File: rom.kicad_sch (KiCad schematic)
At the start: 5 parts, among them IC17 27C256, IC18 74LS08

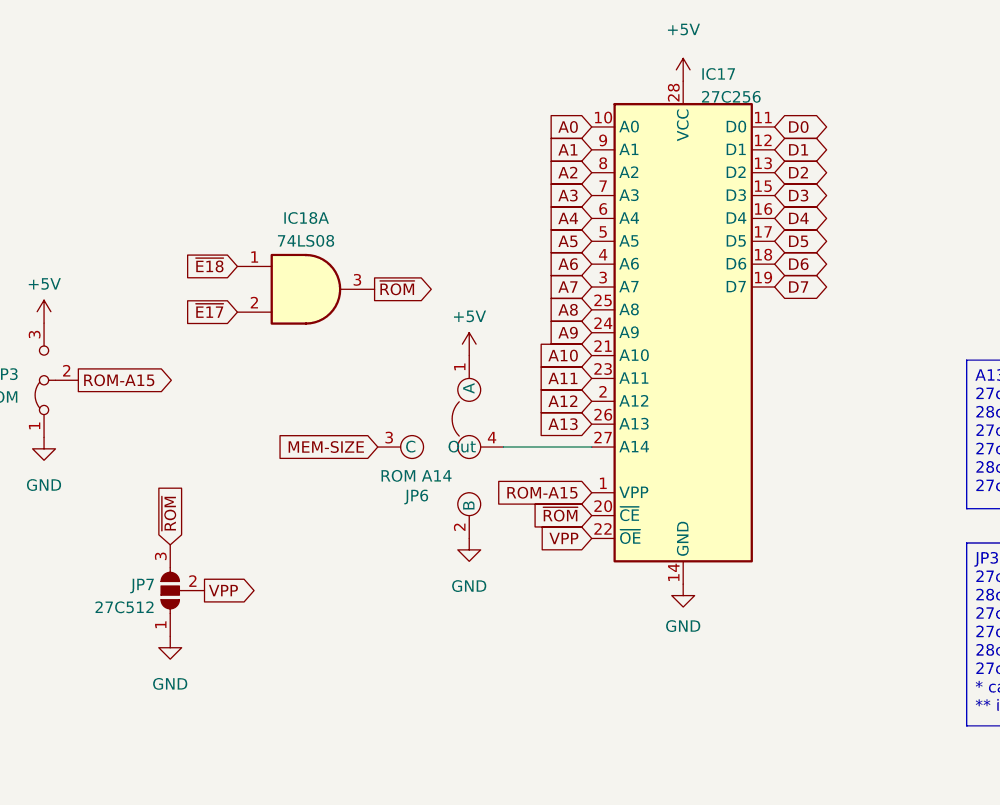
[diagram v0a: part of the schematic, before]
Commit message: rework keyboard type selection
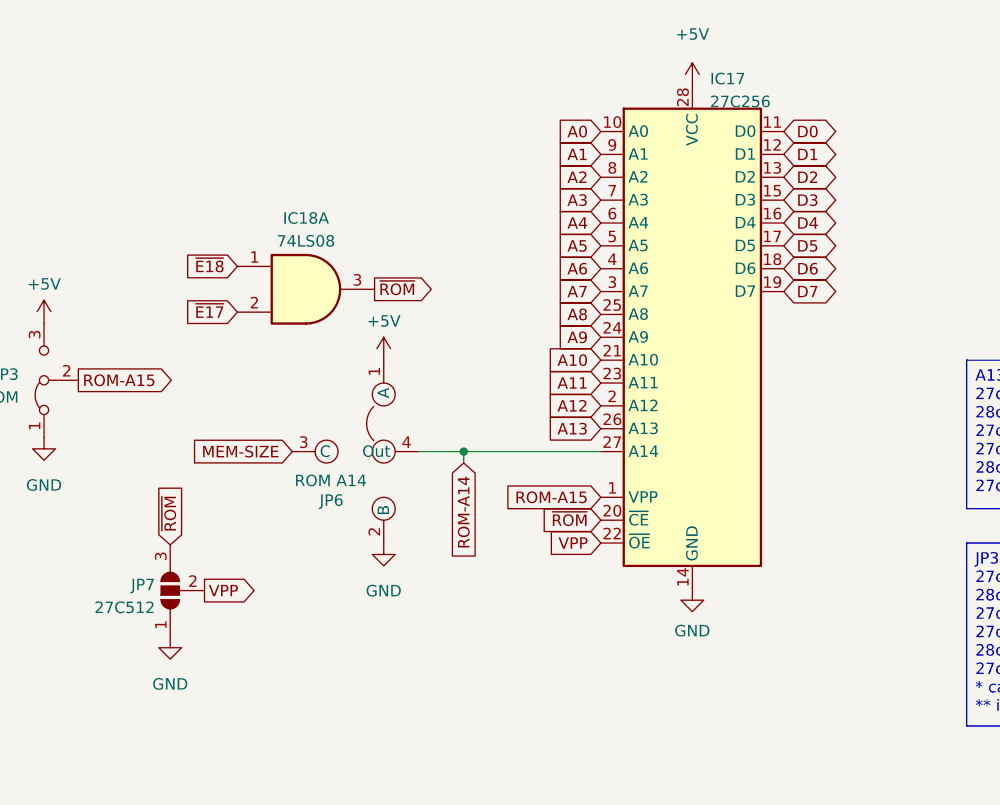
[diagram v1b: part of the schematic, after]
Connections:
- net ROM-A14: now reaches IC17.27 (A14), JP6.4 (Out)
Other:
- moved on the sheet: IC17, JP6

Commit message: refresh BOM
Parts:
- IC18: LCSC (none) -> C22394768
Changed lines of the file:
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@@
+			)
+		)
+		(property "LCSC" "C22394768"
+			(at 387.858 186.944 0)
+			(effects
+				(font
+					(size 1.27 1.27)
+				)
+				(hide yes)
 			)
 		)
@@
 			)
 		)
+		(property "LCSC" "C22394768"
+			(at 91.694 161.036 0)
+			(effects
+				(font
+					(size 1.27 1.27)
+				)
+				(hide yes)
+			)
+		)
 		(pin "1"
 		)
@@
 			)
 		)
+		(property "LCSC" "C22394768"
+			(at 386.334 169.926 0)
+			(effects
+				(font
+					(size 1.27 1.27)
+				)
+				(hide yes)
+			)
+		)
 		(pin "1"
 		)
@@
 		)
 		(property "Description" ""
+			(at 388.874 232.156 0)
+			(effects
+				(font
+					(size 1.27 1.27)
+				)
+				(hide yes)
+			)
+		)
+		(property "LCSC" "C22394768"
 			(at 388.874 232.156 0)
 			(effects
@@
 			(at 389.128 206.756 0)
 			(effects
+				(font
+					(size 1.27 1.27)
+				)
+				(hide yes)
+			)
+		)
+		(property "LCSC" "C22394768"
+			(at 389.128 206.756 0)
+			(effects

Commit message: align versions
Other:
- title: (none) -> Dragon CPU UK Revised
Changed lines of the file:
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@@
 	(paper "A3")
 	(title_block
-		(date "2023-05-25")
-		(rev "3.0")
+		(title "Dragon CPU UK Revised")
+		(date "2025-10-05")
+		(rev "3.3")
+		(comment 1 "Redesign by Julian Brown")
 		(comment 2 "Reposition dram and buffer")
 	)
